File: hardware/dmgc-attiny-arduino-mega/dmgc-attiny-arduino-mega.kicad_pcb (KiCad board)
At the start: 2 copper layers, 101.6 x 53.3 mm, 50 parts, among them J1 Power, J2 Analog, J3 Analog, J4 Digital, J5 PWM, J6 PWM, J7 Communication, SW1 Toggle Flash / Run, SW2 SELECT, SW3 RIGHT, SW4 LEFT, SW5 PUSH, SW6 START/RESET, U1 ATtiny85-20P, U2 Mutex

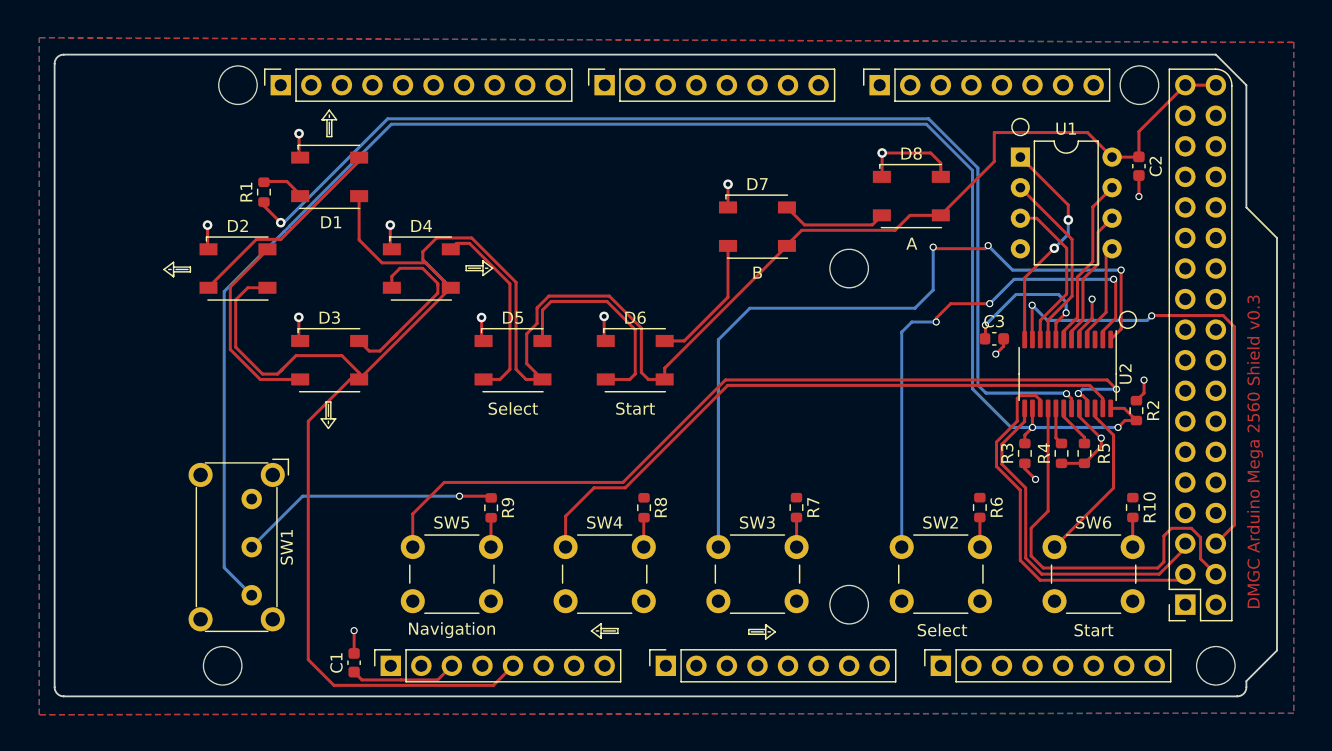
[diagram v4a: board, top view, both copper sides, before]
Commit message: Updated gerbers to v0.4, fixed switch problem with pins reversed. Moved C2 to a better location. Added labels for switch.
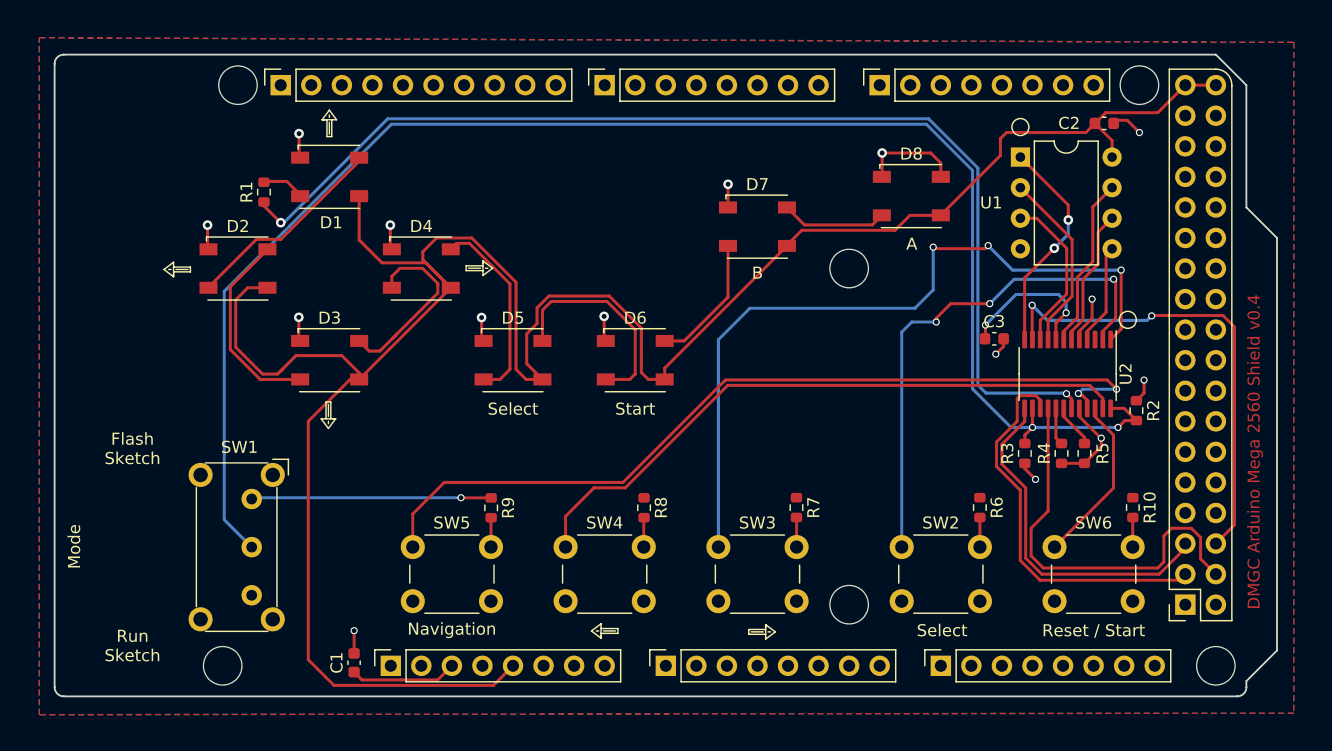
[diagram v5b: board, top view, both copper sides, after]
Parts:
- moved C2 4.58 mm to (187.2, 52.4), turned to 0 degrees
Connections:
- SW1 pad 1: GND -> +3V3
- SW1 pad 2: +3V3 -> Net-(R2-Pad2)
- SW1 pad 3: Net-(R2-Pad2) -> GND
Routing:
- net Net-(R2-Pad2): track 135.8 -> 131.8 mm
- net +3V3: track 34.4 -> 32.6 mm
- net GND: track 43.0 -> 43.6 mm
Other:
- board text added: "DMGC Arduino Mega 2560 Shield v0.4"
- board text added: "Flash Sketch"
- board text added: "Mode"
- board text added: "Reset / Start"
- board text added: "Run Sketch"
- board text removed: "DMGC Arduino Mega 2560 Shield v0.3"
